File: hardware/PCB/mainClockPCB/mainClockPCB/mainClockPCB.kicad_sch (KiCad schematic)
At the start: 54 parts, among them IC1 ESP32-S3-WROOM-1-N16R2, IC2 SPX1117M3-L_TR, IC3 MCP7940N-I_P, IC4 PAM8904QJER, J1 USB_C_Receptacle_USB2.0_16P, J2 Conn_01x09_Socket, J3 Conn_01x02_Socket, SW1 SW_Push, SW2 SW_Push, SW3 SW_Push, SW4 SW_Push, SW5 SW_Push, SW6 SW_Push, SW7 SW_Push, SW8 SW_Push, SW9 SW_Push, U1 PEC11R-4320K-S0012, U2 USBLC6-2SC6, U3 ESP32-S3-WROOM-2, Y1 AB26T-32.768KHZ-6

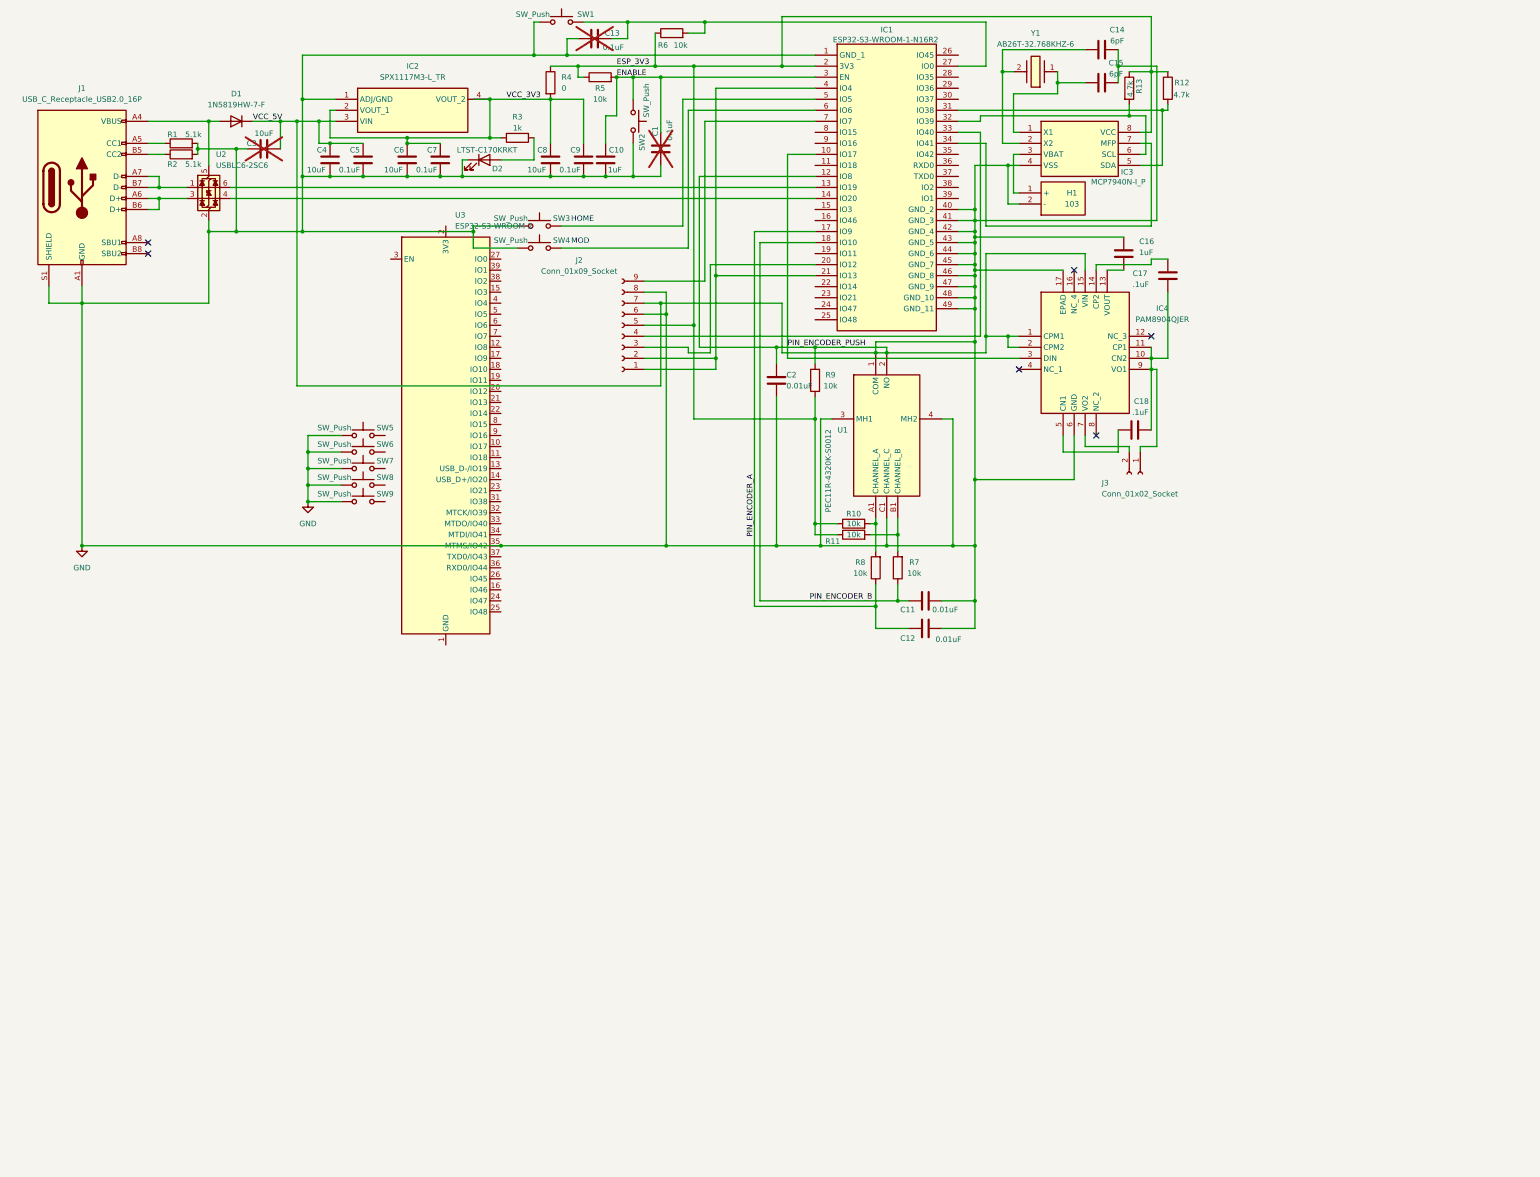
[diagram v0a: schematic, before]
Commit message: clean up of USB, piezo, buttons
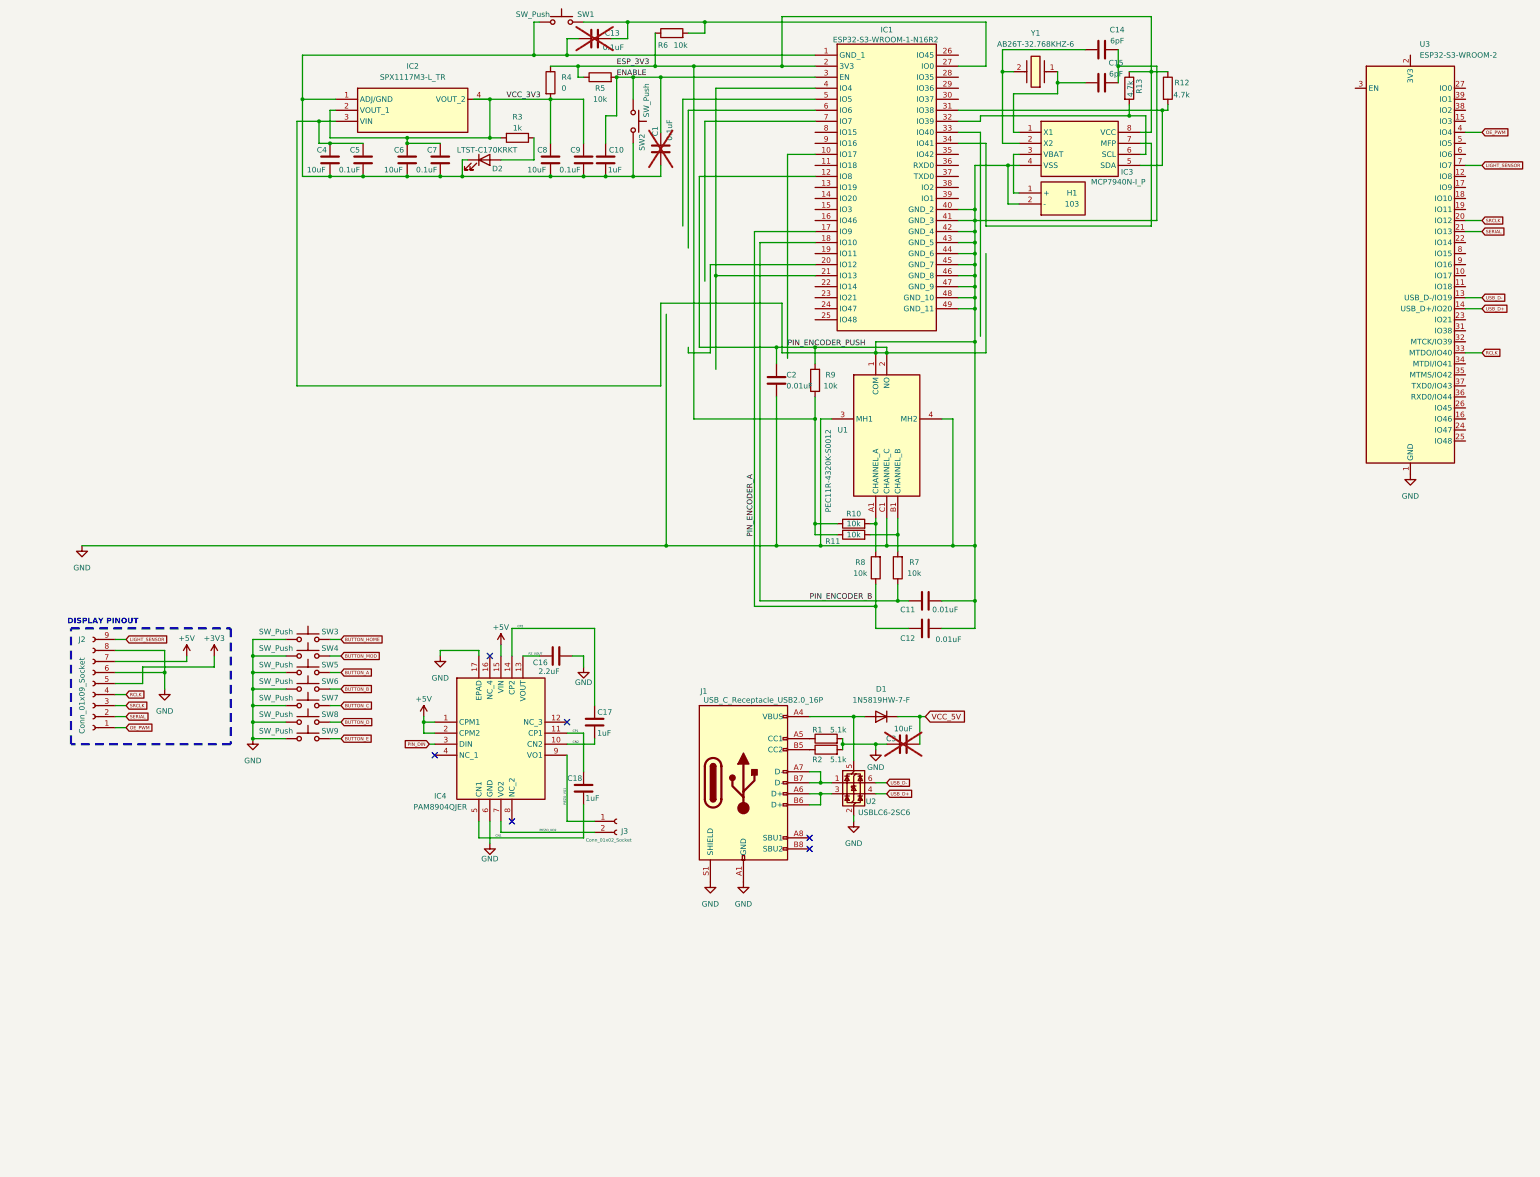
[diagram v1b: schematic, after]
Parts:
- C16: value 1uF -> 2.2uF
- C17, C18: value .1uF -> 1uF
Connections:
- net ESP_3V3: no longer J2.5 (Pin_5)
- net GND: now also C16.2, U3.1 (GND), U3.40 (GND), U3.41 (GND); no longer C1.2, C10.2, C13.2, C16.1, C3.2, C4.2, C5.2, C6.2, C7.2, C8.2, C9.2, D1.1 (K), D2.1 (K), IC1.1 (GND_1), IC2.1 (ADJ/GND), IC4.1 (CPM1), IC4.15 (VIN), IC4.2 (CPM2), IC4.3 (DIN), J2.7 (Pin_7), SW1.1, SW2.2, U3.35 (MTMS/IO42)
- net at IC1.6 (IO6): no longer SW4.2
- net at IC1.21 (IO13), IC1.4 (IO4): no longer J2.1 (Pin_1), J2.2 (Pin_2)
- net at IC1.20 (IO12): no longer J2.3 (Pin_3)
- net at IC1.33 (IO40): no longer J2.4 (Pin_4)
- net at IC1.7 (IO7): no longer J2.9 (Pin_9)
- net PZ_VOUT: now reaches IC4.13 (VOUT)
- net PZ_VOUT: now also C16.1; no longer C16.2
- net CN1: now reaches C18.1, IC4.5 (CN1)
- net CN2: now reaches C17.1
- net CN2: now also IC4.10 (CN2); no longer IC4.14 (CP2)
- net PIEZO_VO2: now reaches IC4.7 (VO2), J3.2 (Pin_2)
- net USB_D-: now reaches U3.13 (USB_D-/IO19)
- net USB_D-: now also U2.6 (I/O1)
- net USB_D+: now reaches U3.14 (USB_D+/IO20)
- net USB_D+: now also U2.4 (I/O2)
- net SRCLK: now reaches U3.20 (IO12)
- net SRCLK: now also J2.3 (Pin_3)
- net SERIAL: now reaches U3.21 (IO13)
- net SERIAL: now also J2.2 (Pin_2)
- net RCLK: now reaches U3.33 (MTDO/IO40)
- net RCLK: now also J2.4 (Pin_4)
- net OE_PWM: now reaches U3.4 (IO4)
- net OE_PWM: now also J2.1 (Pin_1)
- net LIGHT_SENSOR: now reaches U3.7 (IO7)
- net LIGHT_SENSOR: now also J2.9 (Pin_9)
- net BUTTON_B: now reaches SW6.2
- net BUTTON_C: now reaches SW7.2
- net at IC1.14 (IO20): no longer U2.4 (I/O2)
- net at IC1.13 (IO19): no longer U2.6 (I/O1)
- net at IC1.5 (IO5): no longer SW3.2
- net BUTTON_E: now reaches SW9.2
- net BUTTON_D: now reaches SW8.2
- net BUTTON_A: now reaches SW5.2
- new net: C1.2, C10.2, C13.2, C4.2, C5.2, C6.2, C7.2, C8.2, C9.2, D2.1 (K), IC1.1 (GND_1), IC2.1 (ADJ/GND), SW1.1, SW2.2
- new net +3V3: J2.5 (Pin_5)
- new net +5V: IC4.1 (CPM1), IC4.15 (VIN), IC4.2 (CPM2), J2.7 (Pin_7)
- new net BUTTON_HOME: SW3.2
- new net BUTTON_MOD: SW4.2
- new net CP1: C18.2, IC4.11 (CP1)
- new net CP2: C17.2, IC4.14 (CP2)
- new net PIEZO_VO1: IC4.9 (VO1), J3.1 (Pin_1)
- new net PIN_DIN: IC4.3 (DIN)
- new net VCC_5V: C3.2, D1.1 (K)
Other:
- note added: "DISPLAY PINOUT"
- note removed: "HOME"
- note removed: "MOD"
- moved on the sheet: C16, C17, C18, C3, D1, IC4, J1, J2, J3, R1, R2, SW3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

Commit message: previous commit file fix
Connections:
- net +5V: now also C4.1, C5.1, IC2.3 (VIN)
- net ESP_3V3: no longer IC3.8 (VCC), R12.1, R13.1, R4.1
- net GND: now also C14.1, C15.1, C4.2, C5.2, C6.2, C7.2, C8.2, C9.2, D2.1 (K), IC2.1 (ADJ/GND); no longer C14.2, C15.2, C2.1, C4.1, C5.1, IC1.10 (IO17), IC1.12 (IO8), IC2.3 (VIN), R9.2, U1.2 (NO)
- net VCC_3V3: now also R3.1, R4.1; no longer R3.2, R4.2
- net at D2.2 (A): now also R3.2; no longer R3.1
- net SCL: now reaches IC3.6 (SCL), R13.2
- net SCL: no longer IC1.32 (IO39)
- net at IC3.1 (X1), Y1.1: now also C15.2; no longer C15.1
- net at IC3.2 (X2), Y1.2: now also C14.2; no longer C14.1
- net SDA: now reaches IC3.5 (SDA), R12.2
- net SDA: no longer IC1.31 (IO38)
- net at IC1.34 (IO41): no longer IC3.7 (MFP)
- net MFP: now reaches U3.34 (MTDI/IO41)
- net MFP: now also IC3.7 (MFP)
- net +3V3 renamed ESP_3v3
- net ESP_3v3: now also IC3.8 (VCC), R12.1, R13.1, R4.2
- new net: C13.2, IC1.1 (GND_1), SW1.1
- new net: C1.2, C10.2, SW2.2
- new net PIN_ENCODER_PUSH: C2.1, IC1.10 (IO17), IC1.12 (IO8), R9.2, U1.2 (NO)
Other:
- moved on the sheet: C14, C15, C4, C5, C6, C7, C8, C9, D2, H1, IC2, IC3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

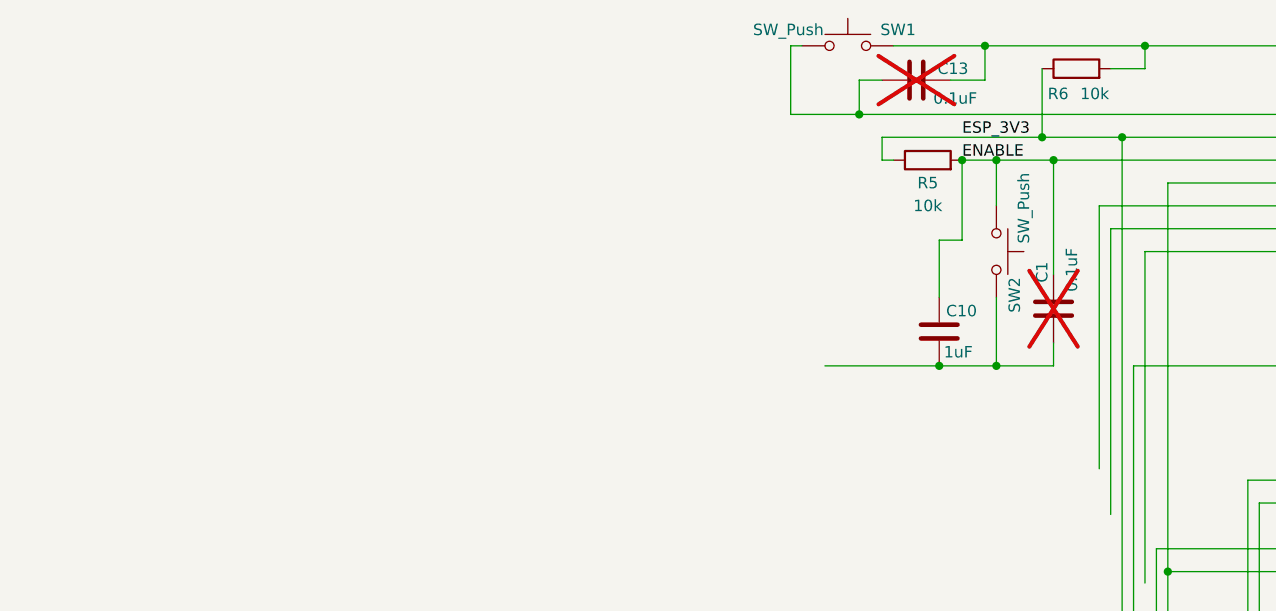
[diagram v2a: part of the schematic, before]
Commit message: enable/boot/reset button schema cleanup
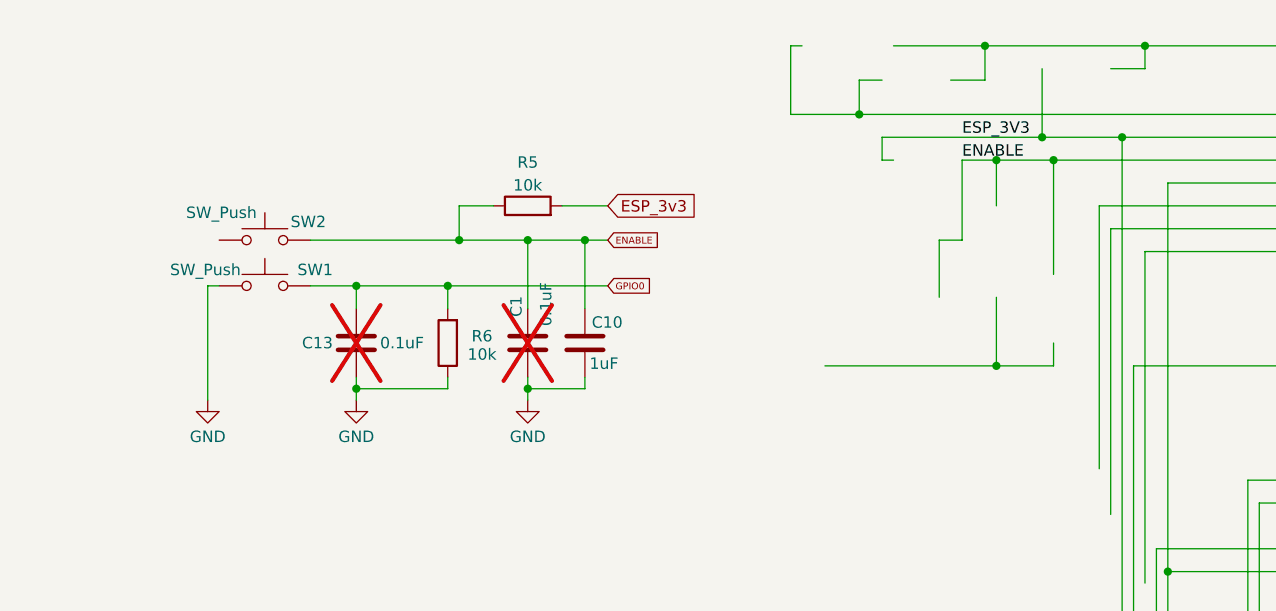
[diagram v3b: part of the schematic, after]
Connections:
- net ENABLE: now also R5.1, SW2.2; no longer R5.2, SW2.1
- net ESP_3V3: no longer R5.1, R6.1
- net ESP_3v3: now also R5.2
- net GND: now also C1.2, C10.2, C13.2, R6.1, SW1.1
- net GPIO0: now reaches C13.1, R6.2, SW1.2
- net GPIO0: no longer IC1.27 (IO0)
- now unconnected: IC1.1 (GND_1)
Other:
- moved on the sheet: C1, C10, C13, R5, R6, SW1, SW2
